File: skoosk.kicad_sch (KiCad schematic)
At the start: 0 parts

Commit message: adding libraries
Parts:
- added F?: Polyfuse_Small, symbol Device:Polyfuse_Small
- added U?: ProMicro, symbol keebio:ProMicro
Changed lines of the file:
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@@
 (kicad_sch (version 20211123) (generator eeschema)
   (paper "A4")
+  (symbol (lib_id "Device:Polyfuse_Small") (at 96.52 154.94 90) (unit 1)
+    (in_bom yes) (on_board yes) (fields_autoplaced)
+    (property "Reference" "F?" (id 0) (at 96.52 148.59 90))
+    (property "Value" "Polyfuse_Small" (id 1) (at 96.52 151.13 90))
+    (property "Footprint" "" (id 2) (at 101.6 153.67 0)
+      (effects (font (size 1.27 1.27)) (justify left) hide)
+    )
+    (property "Datasheet" "~" (id 3) (at 96.52 154.94 0)
+      (effects (font (size 1.27 1.27)) hide)
+    )
+    (pin "1")
+    (pin "2")
+  )
+  (symbol (lib_id "keebio:ProMicro") (at 46.99 163.83 0) (unit 1)
+    (in_bom yes) (on_board yes) (fields_autoplaced)
+    (property "Reference" "U?" (id 0) (at 46.99 142.24 0)
+      (effects (font (size 1.524 1.524)))
+    )
+    (property "Value" "ProMicro" (id 1) (at 46.99 146.05 0)
+      (effects (font (size 1.524 1.524)))
+    )
+    (property "Footprint" "" (id 2) (at 73.66 227.33 90)
+      (effects (font (size 1.524 1.524)) hide)
+    )
+    (property "Datasheet" "" (id 3) (at 73.66 227.33 90)
+      (effects (font (size 1.524 1.524)) hide)
+    )
+    (pin "1")
+    (pin "10")
+    (pin "11")
+    (pin "12")
+    (pin "13")
+    (pin "14")
+    (pin "15")
+    (pin "16")
+    (pin "17")
+    (pin "18")
+    (pin "19")
+    (pin "2")
+    (pin "20")
+    (pin "21")
+    (pin "22")
+    (pin "23")
+    (pin "24")
+    (pin "3")
+    (pin "4")
+    (pin "5")
+    (pin "6")
+    (pin "7")
+    (pin "8")
+    (pin "9")
+  )
   (sheet_instances
     (path "/" (page "1"))
   )
+  (symbol_instances
+    (path "/88fd06e8-4bfc-49e9-a739-700108c41448"
+      (reference "F?") (unit 1) (value "Polyfuse_Small") (footprint "")
+    )
+    (path "/b1d8b9c1-d0cf-460d-9610-64eb34437dc3"
+      (reference "U?") (unit 1) (value "ProMicro") (footprint "")
+    )
+  )
 )

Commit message: switch matrix build, footprints layed out
missing is MCU footprint, reset switch, traces

do i want underglow?
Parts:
- added D1, D10, D11, D12, D13, D14, D15, D16, D17, D18, D19, D2, D20, D21, D22, D23, D24, D25, D26, D27, D28, D29, D3, D30, D31, D32, D33, D34, D35, D36, D37, D38, D39, D4, D40, D41, D42, D43, D44, D5, D6, D7, D8, D9: D_Small, symbol Device:D_Small
- added MX1, MX12, MX13, MX24, MX25, MX36, MX37, MX38, MX39, MX42, MX43, MX44: MX-NoLED, MX_Only:MXOnly-1.25U-NoLED, symbol MX_Alps_Hybrid:MX-NoLED
- added MX10, MX11, MX14, MX15, MX16, MX17, MX18, MX19, MX2, MX20, MX21, MX22, MX23, MX26, MX27, MX28, MX29, MX3, MX30, MX31, MX32, MX33, MX34, MX35, MX4, MX5, MX6, MX7, MX8, MX9: MX-NoLED, MX_Only:MXOnly-1U-NoLED, symbol MX_Alps_Hybrid:MX-NoLED
- added MX40, MX41: MX-NoLED, MX_Only:MXOnly-3U-NoLED, symbol MX_Alps_Hybrid:MX-NoLED
- gave numbers to parts that had none: 2
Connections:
- new net: D25.2 (A), MX25.2 (ROW)
- new net: D16.2 (A), MX16.2 (ROW)
- new net: D43.2 (A), MX43.2 (ROW)
- new net: D9.2 (A), MX9.2 (ROW)
- new net: D24.2 (A), MX24.2 (ROW)
- new net: D1.2 (A), MX1.2 (ROW)
- new net: D21.2 (A), MX21.2 (ROW)
- new net: D12.2 (A), MX12.2 (ROW)
- new net: D17.2 (A), MX17.2 (ROW)
- new net: D23.2 (A), MX23.2 (ROW)
- new net: D42.2 (A), MX42.2 (ROW)
- new net: D4.2 (A), MX4.2 (ROW)
- new net: D8.2 (A), MX8.2 (ROW)
- new net: D3.2 (A), MX3.2 (ROW)
- new net: D26.2 (A), MX26.2 (ROW)
- new net: D44.2 (A), MX44.2 (ROW)
- new net: D5.2 (A), MX5.2 (ROW)
- new net: D2.2 (A), MX2.2 (ROW)
- new net: D10.2 (A), MX10.2 (ROW)
- new net: D11.2 (A), MX11.2 (ROW)
- new net: D33.2 (A), MX33.2 (ROW)
- new net: D20.2 (A), MX20.2 (ROW)
- new net: D29.2 (A), MX29.2 (ROW)
- new net: D27.2 (A), MX27.2 (ROW)
- new net: D28.2 (A), MX28.2 (ROW)
- new net: D35.2 (A), MX35.2 (ROW)
- new net: D7.2 (A), MX7.2 (ROW)
- new net: D30.2 (A), MX30.2 (ROW)
- new net: D38.2 (A), MX38.2 (ROW)
- new net: D19.2 (A), MX19.2 (ROW)
- new net: D41.2 (A), MX41.2 (ROW)
- new net: D37.2 (A), MX37.2 (ROW)
- new net: D15.2 (A), MX15.2 (ROW)
- new net: D14.2 (A), MX14.2 (ROW)
- new net: D31.2 (A), MX31.2 (ROW)
- new net: D13.2 (A), MX13.2 (ROW)
- new net: D18.2 (A), MX18.2 (ROW)
- new net: D34.2 (A), MX34.2 (ROW)
- new net: D22.2 (A), MX22.2 (ROW)
- new net: D6.2 (A), MX6.2 (ROW)
- new net: D36.2 (A), MX36.2 (ROW)
- new net: D40.2 (A), MX40.2 (ROW)
- new net: D39.2 (A), MX39.2 (ROW)
- new net: D32.2 (A), MX32.2 (ROW)
- new net COL0: MX1.1 (COL), MX13.1 (COL), MX14.1 (COL), MX2.1 (COL), MX25.1 (COL), MX26.1 (COL), MX37.1 (COL), MX38.1 (COL)
- new net COL1: MX15.1 (COL), MX16.1 (COL), MX27.1 (COL), MX28.1 (COL), MX3.1 (COL), MX39.1 (COL), MX4.1 (COL)
- new net COL2: MX17.1 (COL), MX18.1 (COL), MX29.1 (COL), MX30.1 (COL), MX40.1 (COL), MX5.1 (COL), MX6.1 (COL)
- new net COL3: MX19.1 (COL), MX20.1 (COL), MX31.1 (COL), MX32.1 (COL), MX41.1 (COL), MX7.1 (COL), MX8.1 (COL)
- new net COL4: MX10.1 (COL), MX21.1 (COL), MX22.1 (COL), MX33.1 (COL), MX34.1 (COL), MX42.1 (COL), MX9.1 (COL)
- new net COL5: MX11.1 (COL), MX12.1 (COL), MX23.1 (COL), MX24.1 (COL), MX35.1 (COL), MX36.1 (COL), MX43.1 (COL), MX44.1 (COL)
- new net ROW0: D1.1 (K), D11.1 (K), D3.1 (K), D5.1 (K), D7.1 (K), D9.1 (K)
- new net ROW1: D10.1 (K), D12.1 (K), D2.1 (K), D4.1 (K), D6.1 (K), D8.1 (K)
- new net ROW2: D13.1 (K), D15.1 (K), D17.1 (K), D19.1 (K), D21.1 (K), D23.1 (K)
- new net ROW3: D14.1 (K), D16.1 (K), D18.1 (K), D20.1 (K), D22.1 (K), D24.1 (K)
- new net ROW4: D25.1 (K), D27.1 (K), D29.1 (K), D31.1 (K), D33.1 (K), D35.1 (K)
- new net ROW5: D26.1 (K), D28.1 (K), D30.1 (K), D32.1 (K), D34.1 (K), D36.1 (K)
- new net ROW6: D37.1 (K), D39.1 (K), D41.1 (K), D43.1 (K)
- new net ROW7: D38.1 (K), D40.1 (K), D42.1 (K), D44.1 (K)
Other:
- moved on the sheet: U1

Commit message: all switches and diodes placed
next change mcu for usb c, figure out a reset button
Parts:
- D1, D10, D11, D12, D13, D14, D15, D16, D17, D18, D19, D2, D20, D21, D22, D23, D24, D25, D26, D27, D28, D29, D3, D30, D31, D32, D33, D34, D35, D36, D37, D38, D39, D4, D40, D41, D42, D43, D44, D5, D6, D7, D8, D9: footprint (none) -> Diode_THT:D_DO-35_SOD27_P7.62mm_Horizontal
- U1: footprint (none) -> kbd:ProMicro_v3.5

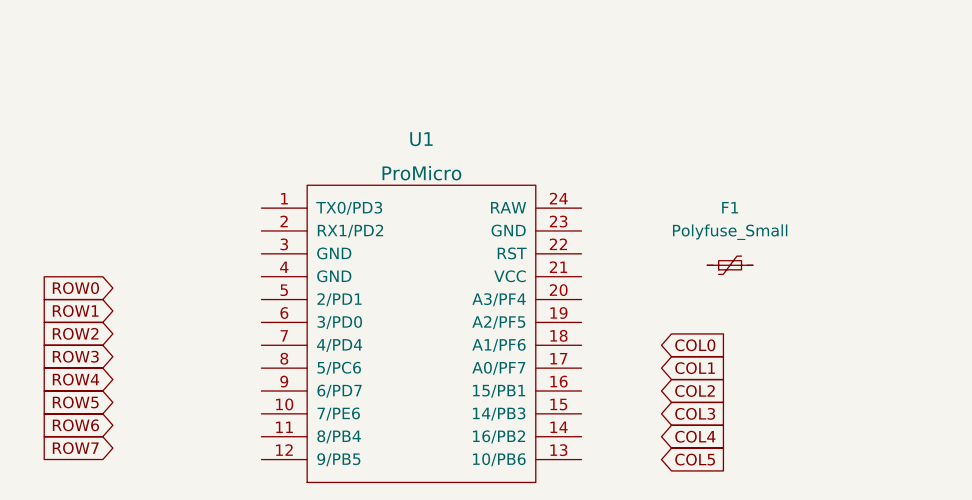
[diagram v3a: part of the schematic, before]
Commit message: tracing col and rows
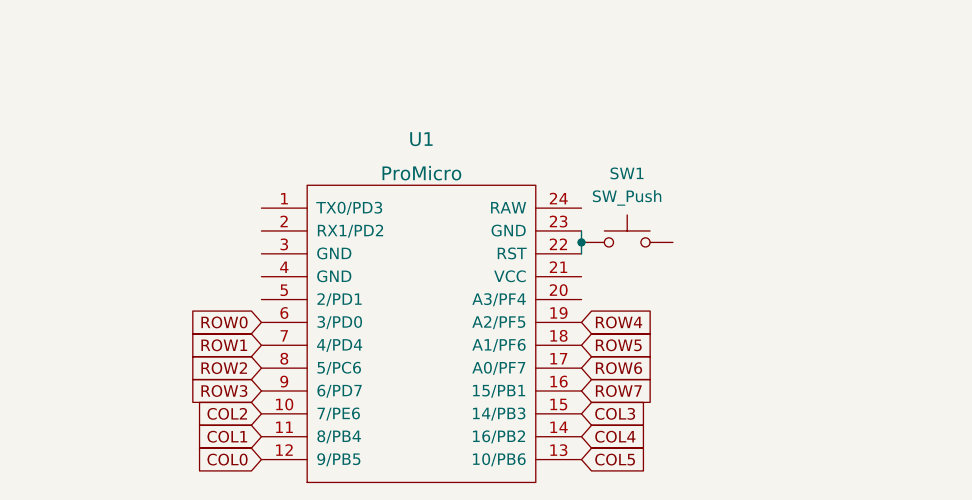
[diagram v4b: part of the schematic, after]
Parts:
- removed F1: Polyfuse_Small, symbol Device:Polyfuse_Small
- added SW1: SW_Push, random-keyboard-parts:SKQG-1155865, symbol Switch:SW_Push
- U1: footprint kbd:ProMicro_v3.5 -> Keebio-Parts:ArduinoProMicro
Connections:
- net COL0: now also U1.12 (9/PB5)
- net COL1: now also U1.11 (8/PB4)
- net COL2: now also U1.10 (7/PE6)
- net COL3: now also U1.15 (14/PB3)
- net COL4: now also U1.14 (16/PB2)
- net COL5: now also U1.13 (10/PB6)
- net ROW0: now also U1.6 (3/PD0)
- net ROW1: now also U1.7 (4/PD4)
- net ROW2: now also U1.8 (5/PC6)
- net ROW3: now also U1.9 (6/PD7)
- net ROW4: now also U1.19 (A2/PF5)
- net ROW5: now also U1.18 (A1/PF6)
- net ROW6: now also U1.17 (A0/PF7)
- net ROW7: now also U1.16 (15/PB1)
- net at U1.22 (RST): now also U1.23 (GND), SW1.1

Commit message: saving before doing autorouting
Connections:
- net COL1: now also U1.10 (7/PE6); no longer U1.11 (8/PB4)
- net COL2: now also U1.11 (8/PB4); no longer U1.10 (7/PE6)
- net COL3: now also U1.13 (10/PB6); no longer U1.15 (14/PB3)
- net COL5: now also U1.15 (14/PB3); no longer U1.13 (10/PB6)
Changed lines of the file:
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@@
     )
   )
-  (global_label "COL1" (shape input) (at 44.45 173.99 180) (fields_autoplaced)
+  (global_label "COL1" (shape input) (at 44.45 171.45 180) (fields_autoplaced)
     (effects (font (size 1.27 1.27)) (justify right))
-    (property "Intersheet References" "${INTERSHEET_REFS}" (id 0) (at 37.1988 174.0694 0)
+    (property "Intersheet References" "${INTERSHEET_REFS}" (id 0) (at 37.1988 171.5294 0)
       (effects (font (size 1.27 1.27)) (justify right) hide)
     )
@@
     )
   )
-  (global_label "COL5" (shape input) (at 80.01 176.53 0) (fields_autoplaced)
+  (global_label "COL5" (shape input) (at 80.01 171.45 0) (fields_autoplaced)
     (effects (font (size 1.27 1.27)) (justify left))
-    (property "Intersheet References" "${INTERSHEET_REFS}" (id 0) (at 87.2612 176.4506 0)
+    (property "Intersheet References" "${INTERSHEET_REFS}" (id 0) (at 87.2612 171.3706 0)
       (effects (font (size 1.27 1.27)) (justify left) hide)
     )
@@
     )
   )
-  (global_label "COL3" (shape input) (at 80.01 171.45 0) (fields_autoplaced)
+  (global_label "COL3" (shape input) (at 80.01 176.53 0) (fields_autoplaced)
     (effects (font (size 1.27 1.27)) (justify left))
-    (property "Intersheet References" "${INTERSHEET_REFS}" (id 0) (at 87.2612 171.3706 0)
+    (property "Intersheet References" "${INTERSHEET_REFS}" (id 0) (at 87.2612 176.4506 0)
       (effects (font (size 1.27 1.27)) (justify left) hide)
     )
@@
     )
   )
-  (global_label "COL2" (shape input) (at 44.45 171.45 180) (fields_autoplaced)
+  (global_label "COL2" (shape input) (at 44.45 173.99 180) (fields_autoplaced)
     (effects (font (size 1.27 1.27)) (justify right))
-    (property "Intersheet References" "${INTERSHEET_REFS}" (id 0) (at 37.1988 171.5294 0)
+    (property "Intersheet References" "${INTERSHEET_REFS}" (id 0) (at 37.1988 174.0694 0)
       (effects (font (size 1.27 1.27)) (justify right) hide)
     )

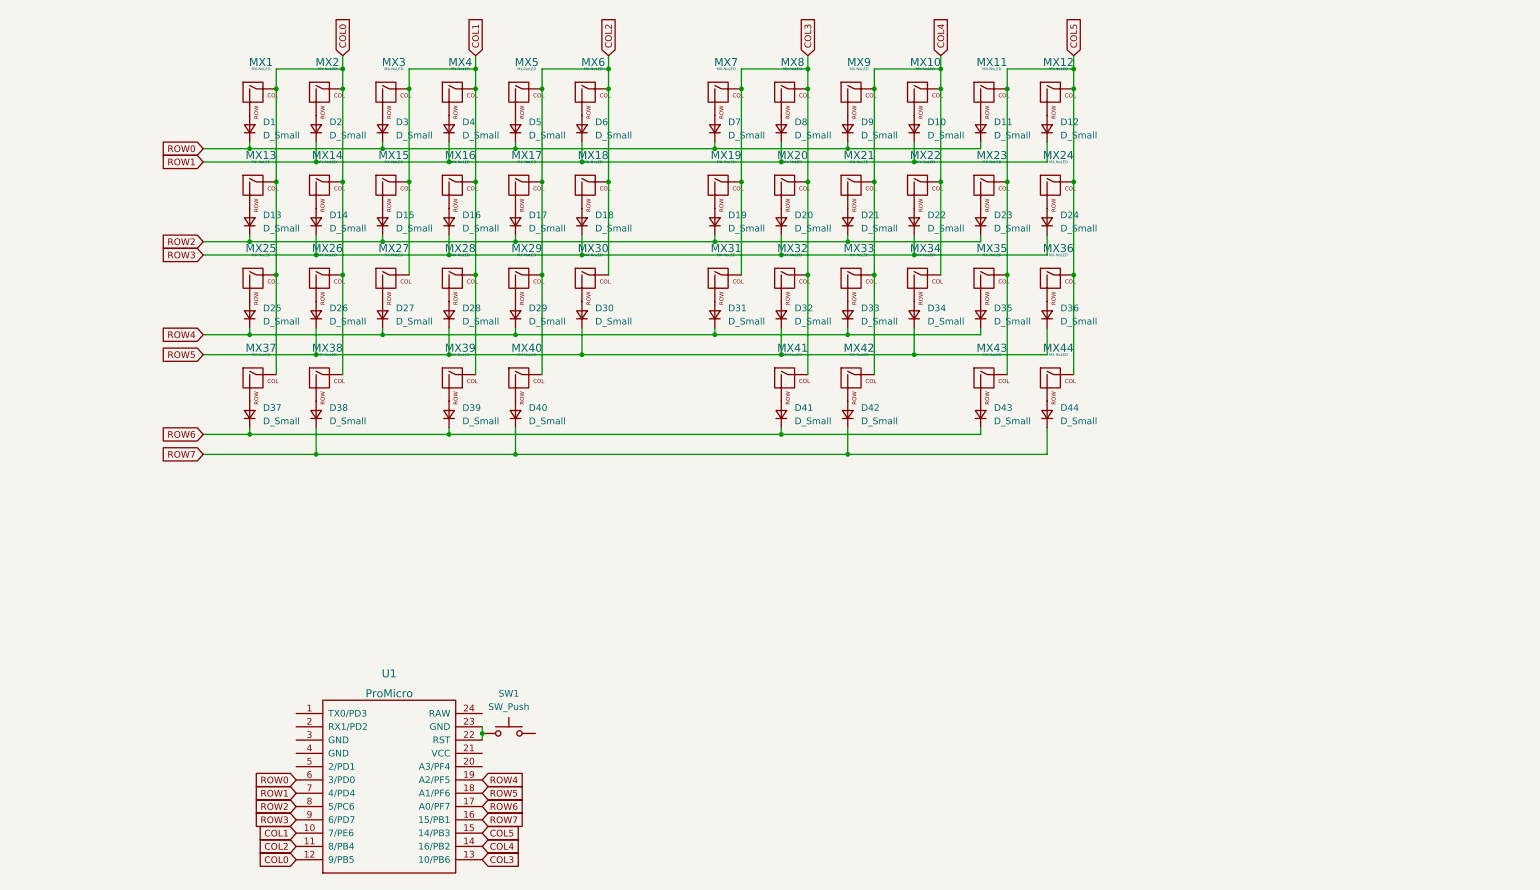
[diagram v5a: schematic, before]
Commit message: added silkscreen, protective layer, auto tracing
auto tracing still needs to be confirmed working
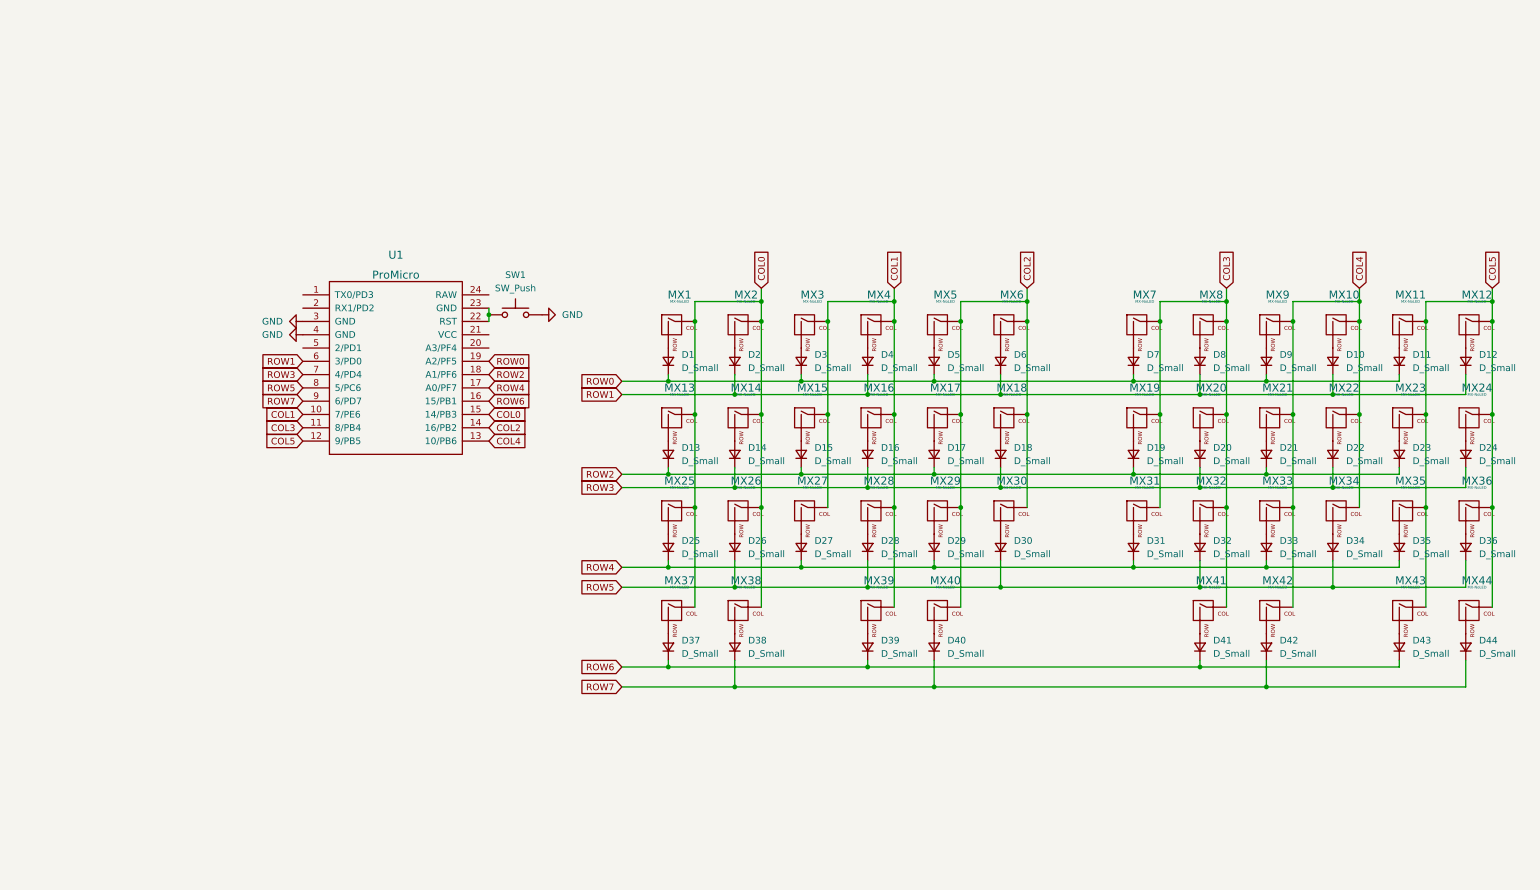
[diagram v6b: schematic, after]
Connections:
- net COL0: now also U1.15 (14/PB3); no longer U1.12 (9/PB5)
- net COL2: now also U1.14 (16/PB2); no longer U1.11 (8/PB4)
- net COL3: now also U1.11 (8/PB4); no longer U1.13 (10/PB6)
- net COL4: now also U1.13 (10/PB6); no longer U1.14 (16/PB2)
- net COL5: now also U1.12 (9/PB5); no longer U1.15 (14/PB3)
- net ROW0: now also U1.19 (A2/PF5); no longer U1.6 (3/PD0)
- net ROW1: now also U1.6 (3/PD0); no longer U1.7 (4/PD4)
- net ROW2: now also U1.18 (A1/PF6); no longer U1.8 (5/PC6)
- net ROW3: now also U1.7 (4/PD4); no longer U1.9 (6/PD7)
- net ROW4: now also U1.17 (A0/PF7); no longer U1.19 (A2/PF5)
- net ROW5: now also U1.8 (5/PC6); no longer U1.18 (A1/PF6)
- net ROW6: now also U1.16 (15/PB1); no longer U1.17 (A0/PF7)
- net ROW7: now also U1.9 (6/PD7); no longer U1.16 (15/PB1)
- net GND: now reaches SW1.2
- net GND: now also U1.3 (GND), U1.4 (GND)
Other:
- moved on the sheet: D1, D10, D11, D12, D13, D14, D15, D16, D17, D18, D19, D2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
